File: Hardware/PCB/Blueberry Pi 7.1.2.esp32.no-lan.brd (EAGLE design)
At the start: 80.7 x 61.3 mm, 190 parts, among them IC2 E73_2G4M04S, J2 AUDIO_JACK_SMD, J3 USB-A-FEMALE, Q1 24Mhz, Q2 32kHz, Q3 IRLML2402, Q4 IRLML2402, U1 SN65LVDS84AQDGGRQ1, U2 W25Q32FV, U3 AP3031KTR-G1, U4 ESP-WROOM-32, X1 FH12-50S-0.5SH, X2 87758-1216

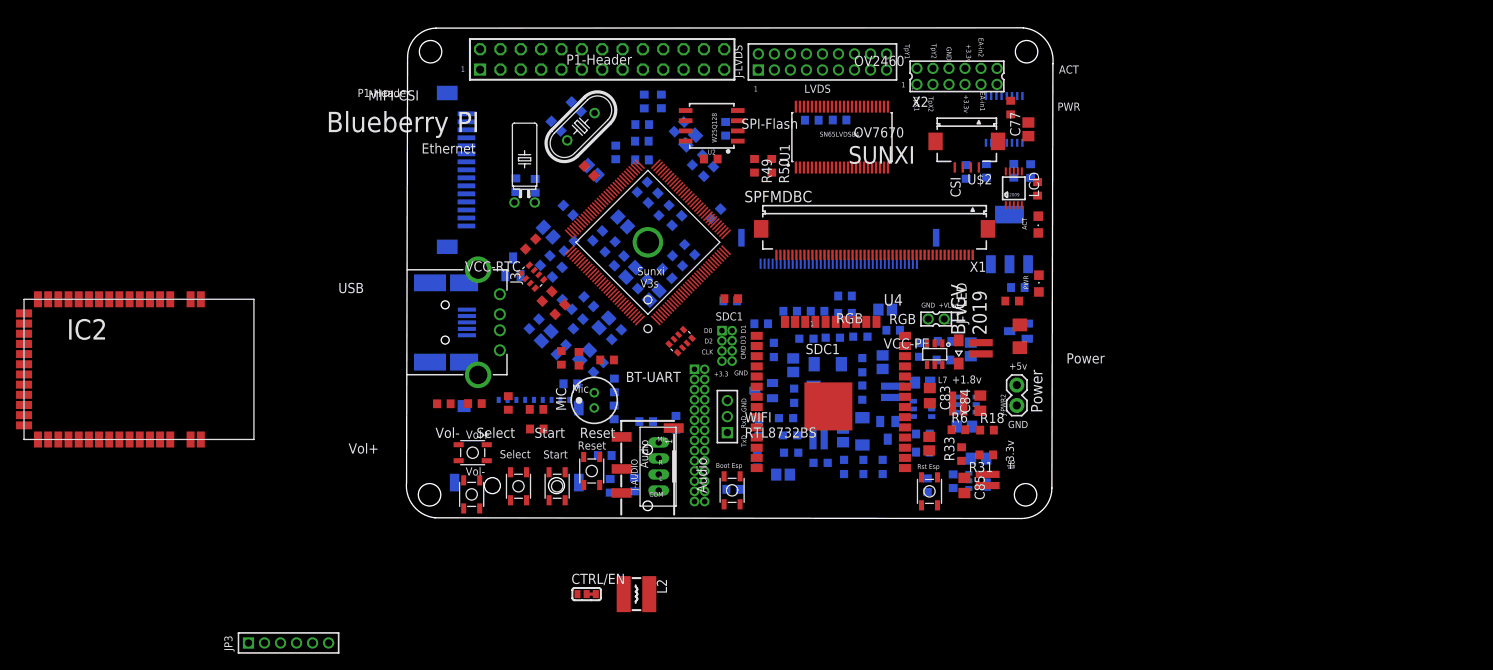
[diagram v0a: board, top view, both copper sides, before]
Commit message: added onboard li-ion/polimer battery charger, and step-up circuits for power from a li-battery.
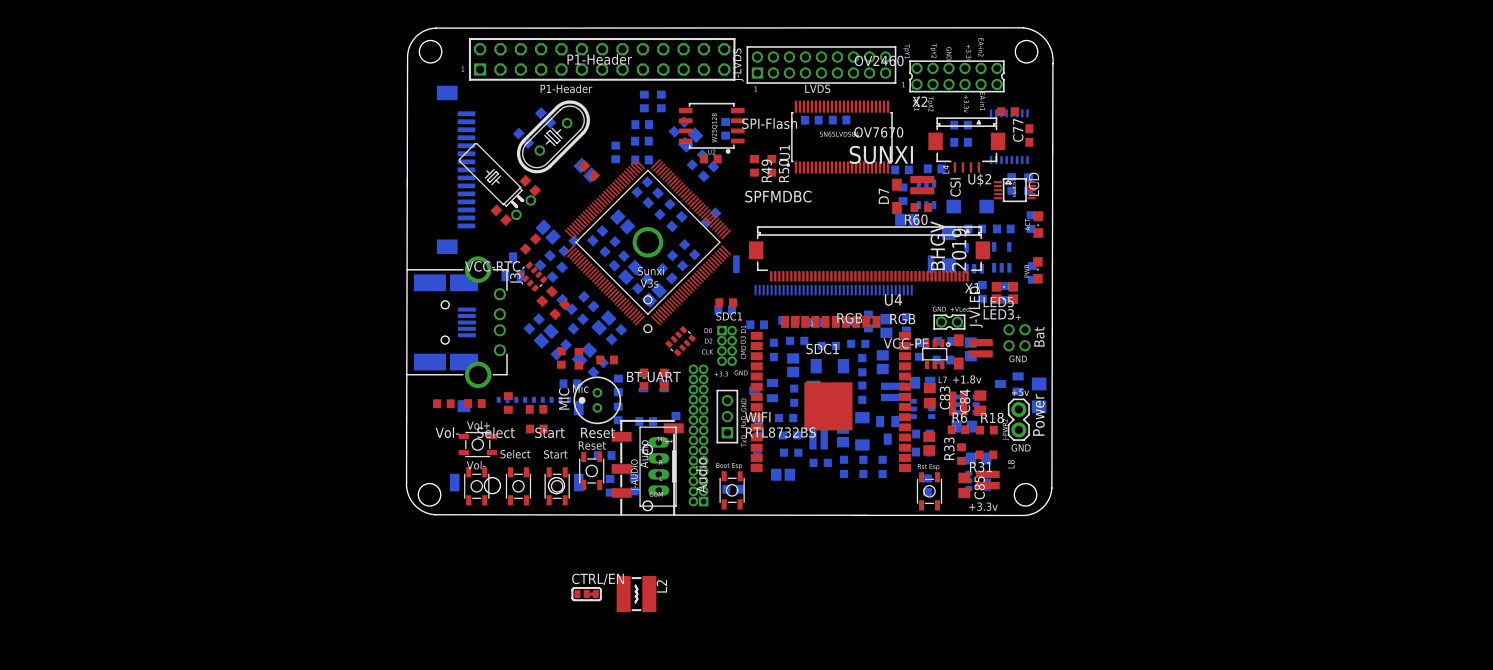
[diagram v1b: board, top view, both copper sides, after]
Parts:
- removed IC1: (no value), v-reg-2:SOT223
- removed IC2: E73_2G4M04S, E73-2G4M04S:E73_2G4M04S
- removed JP3: (no value), pinhead-1:1X06M
- removed R24: 6k 1%, rcl:R0603
- added C44: 10µF, rcl:C0805
- added D2, D6: (no value), diode:DO214AC
- added D7: (no value), diode:SOD323-W
- added J-BAT: 87758-0416, con-molex:87758-0416
- added L4: 2,2µH, rcl:ODD-INDUCTOR
- added LED3, LED5: (no value), led:CHIPLED_0805
- added R53, R58: 2k, rcl:R0603
- added R54, R57, R59: 1k, rcl:R0603
- added R55: 10k, rcl:R0603
- added R56: 15k, rcl:R0603
- added R60: 47k, rcl:R0603
- added U$10: PT4101, PT4101:SOT23-6
- added U$14, U$6: MCP73831, mcp73831:SOT23-5L
- added U$15: XC6204, XC6204:SOT25
- C77: device resistor:C0805 -> resistor:C0603
- moved C37 48.1 mm to (41.1, 17.4), flipped to the top, turned to 270 degrees
- moved C36 38.2 mm to (43.6, 17.4), flipped to the top, turned to 270 degrees
- moved F1 7.75 mm to (90.4, 15.4), flipped to the bottom
- moved Q3 6.70 mm to (86.7, 16.8)
- moved R43 6.54 mm to (80.6, 49.1), turned to 180 degrees
- moved C12 4.34 mm to (26.0, 47.5)
- moved R16 4.32 mm to (89.5, 30.7), flipped to the bottom, turned to 90 degrees
- moved R9 4.31 mm to (69.1, 24.6), turned to 90 degrees
- moved R17 4.23 mm to (89.4, 37.0), flipped to the bottom, turned to 270 degrees
- moved C8 4.17 mm to (23.2, 37.9), flipped to the top, turned to 135 degrees
- moved C11 4.06 mm to (28.8, 50.0)
- moved R48 3.74 mm to (80.6, 47.0), turned to 180 degrees
- moved Q1 3.66 mm to (29.8, 47.7)
- moved J-LCD-FFC 3.36 mm to (64.7, 31.7)
- moved J-PWR2 3.06 mm to (87.9, 11.1)
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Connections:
- removed net +3V3ANC: IC1.4
- removed net DCC: IC2.13
- removed net DEC1: IC2.14
- removed net DEC2: IC2.3
- removed net DEC3: IC2.4
- removed net DEC4: IC2.12
- removed net EPHY_RXN: U$1.89
- removed net EPHY_RXP: U$1.90
- removed net EPHY_TXN: U$1.91
- removed net EPHY_TXP: U$1.92
- removed net LINK_LED: U$1.77
- removed net N$1: R24.1, U$1.94
- removed net SPD_LED: U$1.78
- new net N$12: R55.1, R59.1, U$10.4
- new net N$13: D7.A, L4.P$2, U$10.1
- new net N$14: C44.1, U$10.6
- new net N$19: R53.2, U$6.5
- new net N$35: LED3.C, R54.1
- new net N$38: R54.2, U$6.1
- new net N$4: D2.C, D6.C, L4.P$1, R59.2
- new net N$46: R58.2, U$14.5
- new net N$50: R57.2, U$14.1
- new net N$51: LED5.C, R57.1
- new net N$7: R56.1, R60.1, U$10.3
- new net VIB1: U$7.7, X2.11
- new net VIB2: U$7.8, X2.12
- new net V_BAT1: D2.A, J-BAT.3, U$6.3
- new net V_BAT2: D6.A, J-BAT.1, U$14.3
- net +3V3A: now also U$15.5; no longer IC1.2
- net +5V: now also D7.C, R60.2, U$10.5, U$15.1, U$15.3; no longer IC1.3
- net GND: now also C44.2, J-BAT.2, J-BAT.4, R53.1, R55.2, R56.2, R58.1, U$10.2, U$14.2, U$15.2, U$6.2; no longer IC1.1, R24.2
- net V_PWR: now also LED3.A, LED5.A, U$14.4, U$6.4
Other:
- board size 80.7 x 61.3 mm -> 80.7 x 60.9 mm
- board text added: "+"
- board text added: "Bat"
- board text removed: "Blueberry PI"
- board text removed: "Ethernet"
- board text removed: "USB"

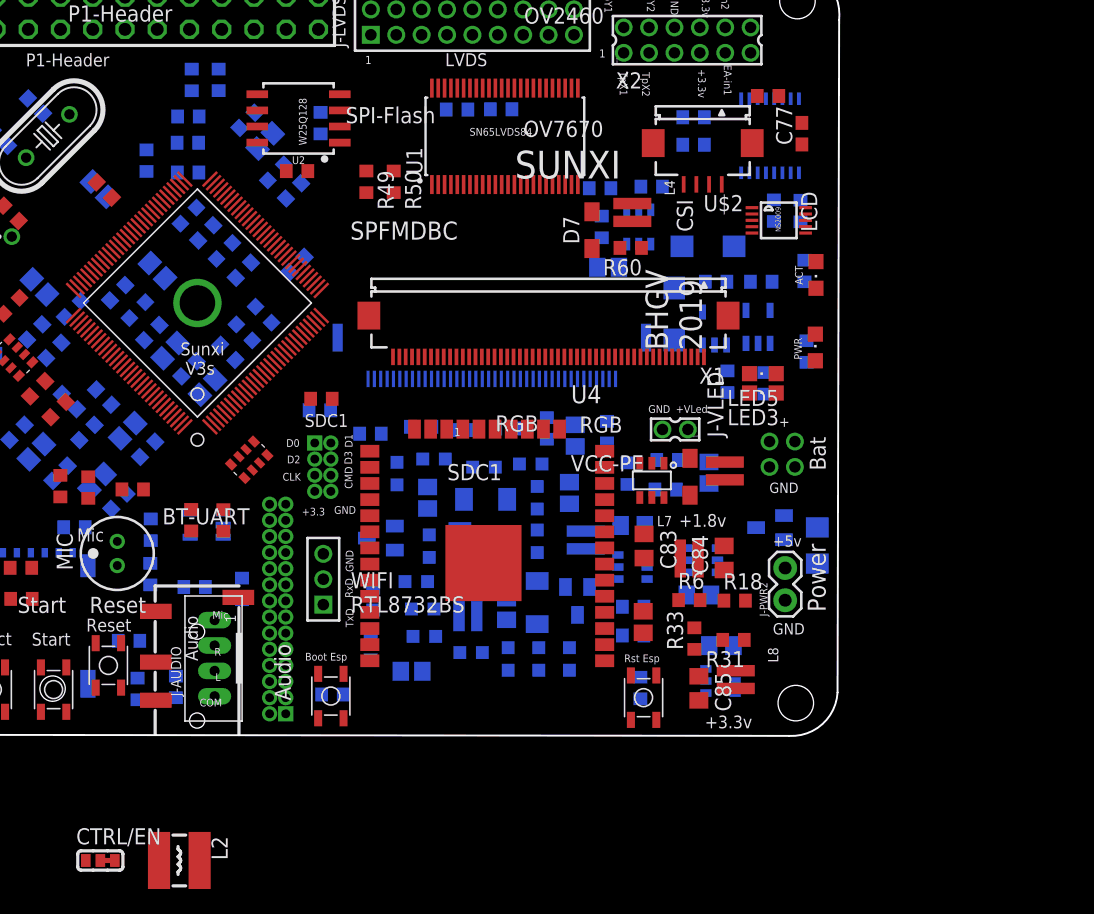
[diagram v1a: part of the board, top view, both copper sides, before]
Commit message: added capacitive touch socket (not ready yet), other pwr-inductors (CD32), datasheets
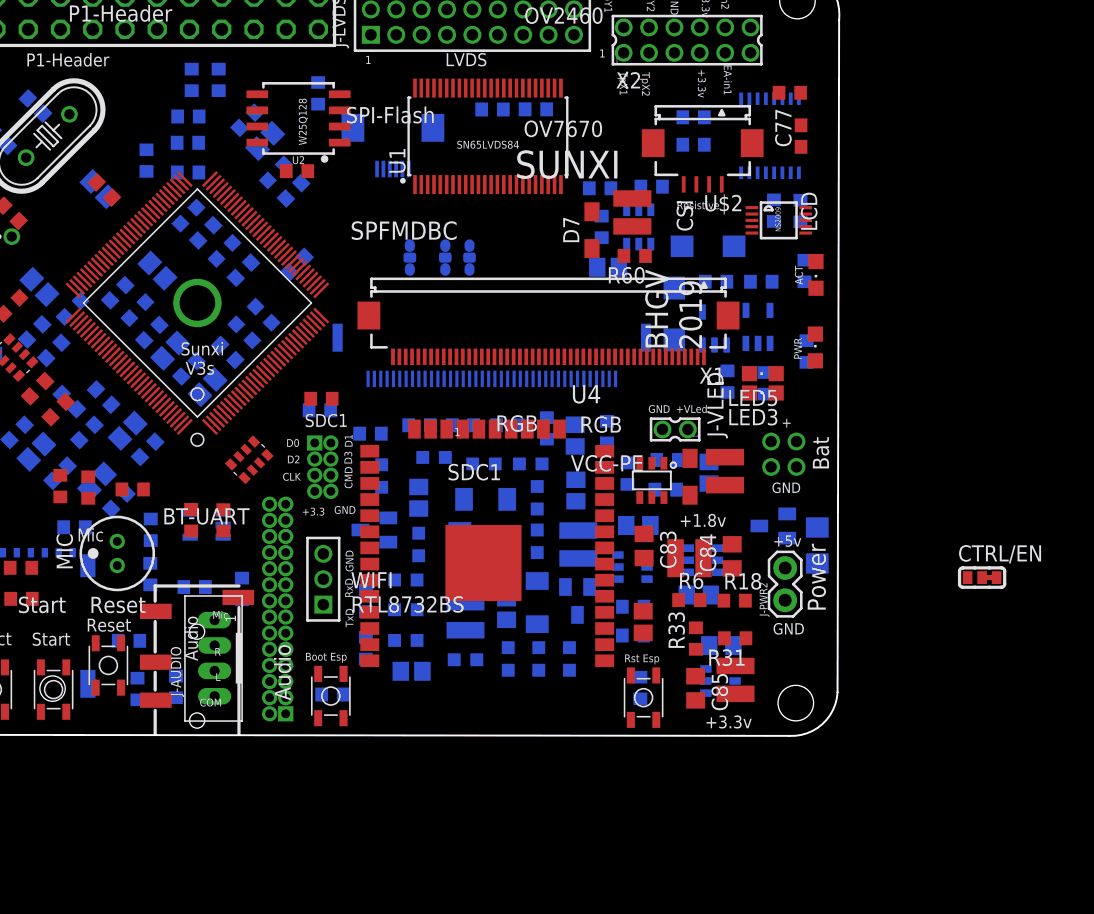
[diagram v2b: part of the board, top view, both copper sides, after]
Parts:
- removed L2: 4.7uH/1.15A/DCR<0.1R/CD43, OLIMEX_DISCRET:CD42(43)
- removed R49: 10k, rcl:R0603
- removed R50: na, rcl:R0603
- added JMP1, JMP2, JMP3: 0R-JUMPC, jump-0r-smd:C0R-JMP
- added U$21: FH12-06S-0.5S, con-hirose:FH12-6S-0.5SH
- L1, L3: value 2,2µH -> 47µH; device rcl:ODD-INDUCTOR -> induct-CD:CD32
- L4: value 2,2µH -> 2.2uH; device rcl:ODD-INDUCTOR -> induct-CD:CD32
- L6, L7, L8: device rcl:ODD-INDUCTOR -> induct-CD:CD32
- moved CTRL/EN 73.0 mm to (103.4, 12.9)
- moved R44 2.79 mm to (64.8, 49.8)
- moved R45 2.73 mm to (68.2, 49.8)
- moved C1 2.36 mm to (51.1, 51.0)
- moved C2 1.73 mm to (88.2, 51.1)
- moved C33 1.49 mm to (58.0, 7.94)
- moved C35 1.34 mm to (58.0, 10.4)
- moved U1 1.33 mm to (64.4, 47.7)
- moved C43 1.22 mm to (56.1, 20.9)
- moved R34 0.84 mm to (58.0, 12.7)
- moved R19 0.84 mm to (59.0, 15.5)
- moved D4 0.81 mm to (55.5, 16.6)
- moved C41 0.72 mm to (62.7, 6.41)
- moved R60 0.71 mm to (76.0, 38.2)
- moved C5 0.70 mm to (59.0, 19.2)
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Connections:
- new net L/R: JMP1.2, X1.39
- new net N$1: U$7.12
- new net N$18: U$7.11
- new net U/D: JMP2.2, X1.40
- net +3V3: now also JMP1.3, JMP2.3, JMP3.1, U$21.2; no longer R49.1
- net GND: now also JMP1.1, JMP2.1, JMP3.3, U$21.3; no longer R50.1
- net I2C1/SCL: now also U$21.6; no longer U$7.12
- net I2C1/SDA: now also U$21.5; no longer U$7.11
- net N$24: now also JMP3.2; no longer R49.2, R50.2
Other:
- board text added: "Capasitive"
- board text added: "Resistive"

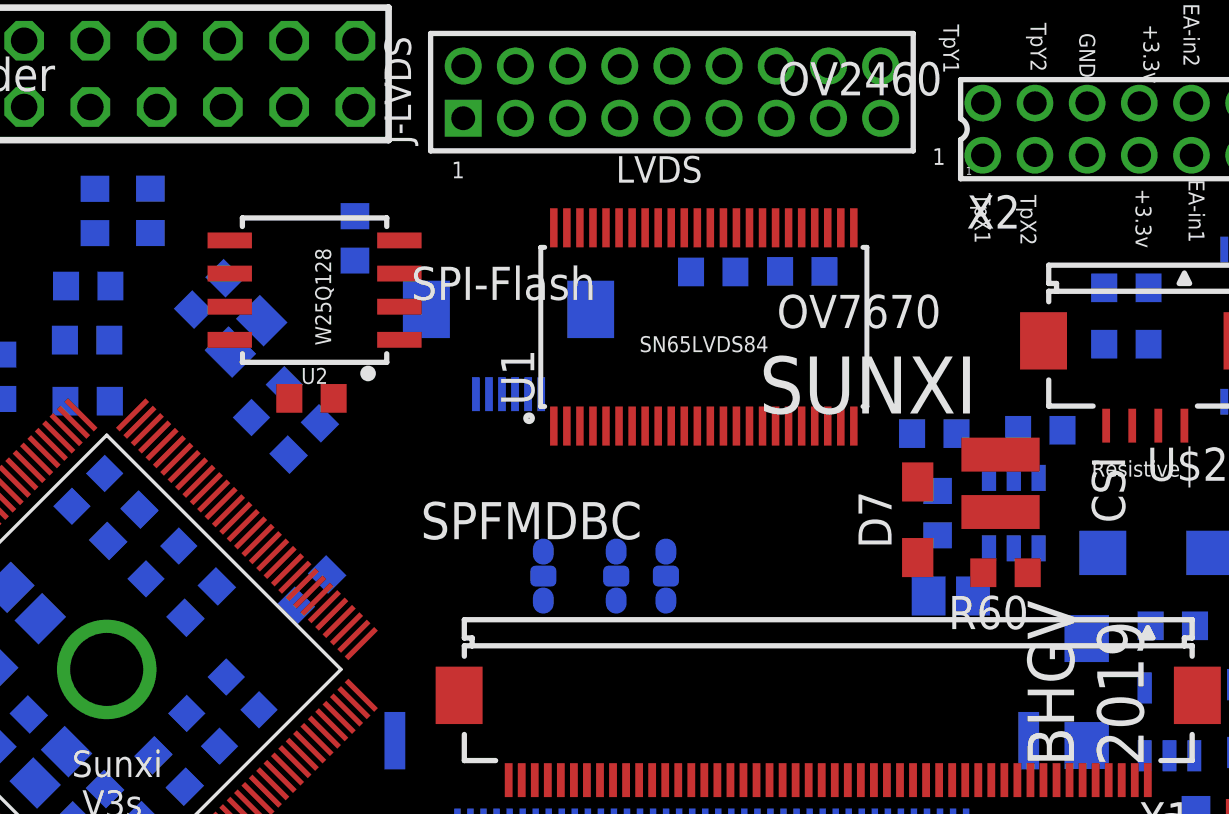
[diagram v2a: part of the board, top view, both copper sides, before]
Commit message: interrupt pin for all touchscreens is PB3 shared with MIPI-CSI cam. basically added SPI-NOR-FLASH in the 16pins package (>= 32MB flashes)
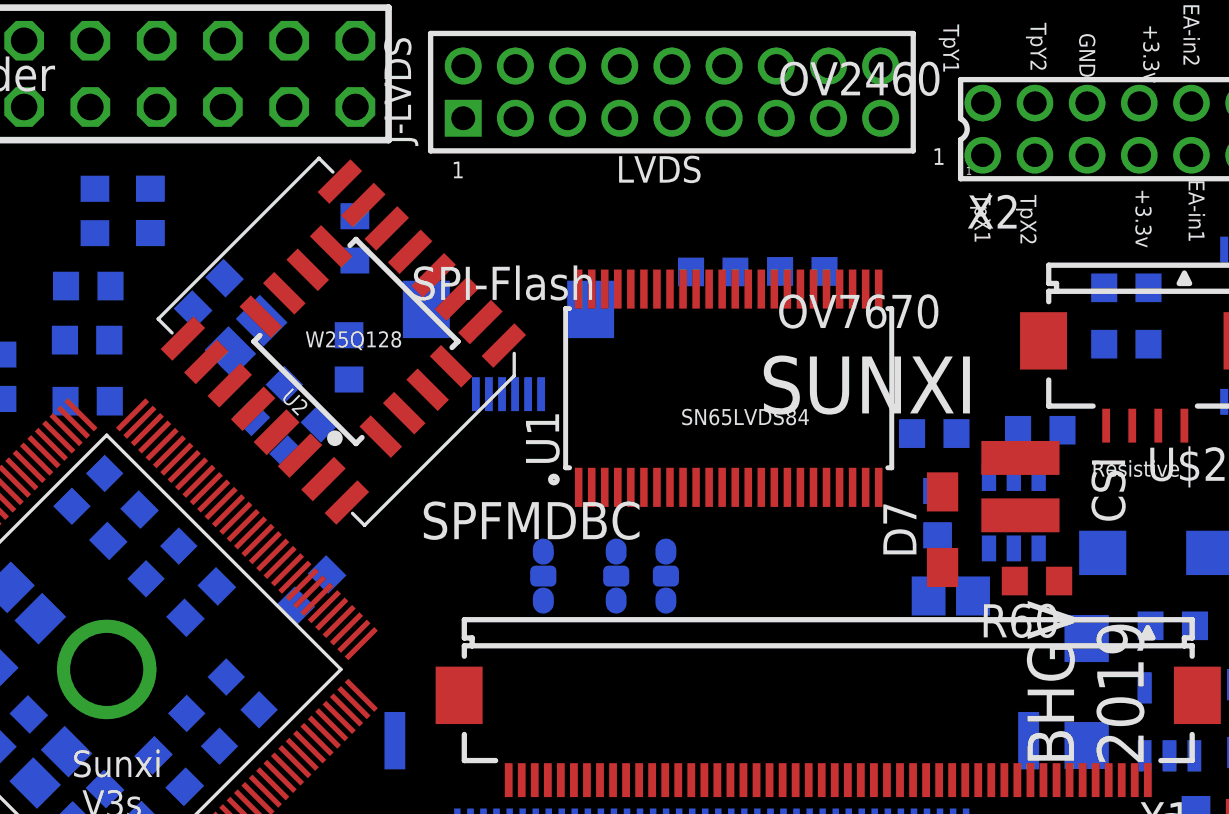
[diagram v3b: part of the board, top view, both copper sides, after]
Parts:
- added U$16: S25FL256S, Synapseware:WSOIC-16
- moved U1 2.54 mm to (65.4, 45.3)
- moved U2 2.53 mm to (51.1, 47.1), turned to 45 degrees
- moved R8 2.13 mm to (50.8, 46.5), flipped to the bottom, turned to 270 degrees
- moved R60 1.25 mm to (77.2, 37.9)
- moved D7 1.03 mm to (73.6, 39.9)
- moved L4 0.77 mm to (76.6, 41.5)
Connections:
- removed net N$1: U$7.12
- removed net N$18: U$7.11
- net +3V3: now also U$16.1, U$16.2, U$16.9
- net GND: now also U$16.10
- net I2C1/SCL: now also U$7.12
- net I2C1/SDA: now also U$7.11
- net PB3: now also U$21.4, U$7.10, U$8.7
- net RESET: now also U$21.1
- net SPI1/CS: now also U$16.7
- net SPI1/MISO: now also U$16.8
- net SPI1/MOSI: now also U$16.15
- net SPI1/SCK: now also U$16.16
